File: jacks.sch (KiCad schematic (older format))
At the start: 73 parts, among them J1 PJ301CM, J10 PJ301BM, J11 PJ301BM, J12 PJ301BM, J13 PJ301BM, J14 PJ301BM, J15 PJ301BM, J16 PJ301BM, J17 PJ301BM, J18 PJ301BM, J19 PJ301BM, J2 PJ301CM, J20 PJ301BM, J21 PJ301BM, J22 PJ301BM, J23 PJ301BM, J24 PJ301BM, J25 PJ301BM, J26 PJ301BM, J3 PJ301BM, J4 PJ301BM, J5 PJ301BM, J6 PJ301BM, J7 PJ301BM, J8 PJ301BM, J9 PJ301BM, Q1 MMBT3904, Q2 MMBT3904, Q3 MMBT3904, Q4 MMBT3904, U1 VO0600T, U2 74LV1T34, U6 MCP6004

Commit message: updated footprints
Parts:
- J1, J2: footprint w_connector:PJ301CM_OFFSET -> w_connector:PJ366ST_Compact
- J10, J11, J12, J13, J14, J15, J16, J17, J18, J19, J20, J21, J22, J23, J24, J25, J26, J3, J4, J5, J6, J7, J8, J9: footprint w_connector:PJ301BM -> w_connector:PJ301M-12_Compact
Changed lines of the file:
@@
 F 0 "J3" H 900 1600 50  0000 C CNN
 F 1 "PJ301BM" H 900 2000 50  0000 C CNN
-F 2 "w_connector:PJ301BM" H 1250 1900 50  0001 C CNN
+F 2 "w_connector:PJ301M-12_Compact" H 1250 1900 50  0001 C CNN
 F 3 "http://www.qingpu-electronics.com/en/products/wqp-pj3010bm-34.html" H 1250 1900 50  0001 C CNN
 F 4 "Wenzhou QingPu Electronics" H 900 1700 50  0001 C CNN "MFN"
@@
 F 0 "J4" H 900 3200 50  0000 C CNN
 F 1 "PJ301BM" H 900 3600 50  0000 C CNN
-F 2 "w_connector:PJ301BM" H 1250 3500 50  0001 C CNN
+F 2 "w_connector:PJ301M-12_Compact" H 1250 3500 50  0001 C CNN
 F 3 "http://www.qingpu-electronics.com/en/products/wqp-pj3010bm-34.html" H 1250 3500 50  0001 C CNN
 F 4 "Wenzhou QingPu Electronics" H 900 3300 50  0001 C CNN "MFN"
@@
 F 0 "J5" H 4700 1300 50  0000 C CNN
 F 1 "PJ301BM" H 4700 1700 50  0000 C CNN
-F 2 "w_connector:PJ301BM" H 5050 1600 50  0001 C CNN
+F 2 "w_connector:PJ301M-12_Compact" H 5050 1600 50  0001 C CNN
 F 3 "http://www.qingpu-electronics.com/en/products/wqp-pj3010bm-34.html" H 5050 1600 50  0001 C CNN
 F 4 "Wenzhou QingPu Electronics" H 4700 1400 50  0001 C CNN "MFN"
@@
 F 0 "J6" H 4700 3000 50  0000 C CNN
 F 1 "PJ301BM" H 4700 3400 50  0000 C CNN
-F 2 "w_connector:PJ301BM" H 5050 3300 50  0001 C CNN
+F 2 "w_connector:PJ301M-12_Compact" H 5050 3300 50  0001 C CNN
 F 3 "http://www.qingpu-electronics.com/en/products/wqp-pj3010bm-34.html" H 5050 3300 50  0001 C CNN
 F 4 "Wenzhou QingPu Electronics" H 4700 3100 50  0001 C CNN "MFN"
@@
 F 0 "J12" H 8800 700 50  0000 C CNN
 F 1 "PJ301BM" H 8800 1100 50  0000 C CNN
-F 2 "w_connector:PJ301BM" H 9150 1000 50  0001 C CNN
+F 2 "w_connector:PJ301M-12_Compact" H 9150 1000 50  0001 C CNN
 F 3 "http://www.qingpu-electronics.com/en/products/wqp-pj3010bm-34.html" H 9150 1000 50  0001 C CNN
 F 4 "Wenzhou QingPu Electronics" H 8800 800 50  0001 C CNN "MFN"
@@
 F 0 "J14" H 8800 1400 50  0000 C CNN
 F 1 "PJ301BM" H 8800 1800 50  0000 C CNN
-F 2 "w_connector:PJ301BM" H 9150 1700 50  0001 C CNN
+F 2 "w_connector:PJ301M-12_Compact" H 9150 1700 50  0001 C CNN
 F 3 "http://www.qingpu-electronics.com/en/products/wqp-pj3010bm-34.html" H 9150 1700 50  0001 C CNN
 F 4 "Wenzhou QingPu Electronics" H 8800 1500 50  0001 C CNN "MFN"
@@
 F 0 "J16" H 8800 2100 50  0000 C CNN
 F 1 "PJ301BM" H 8800 2500 50  0000 C CNN
-F 2 "w_connector:PJ301BM" H 9150 2400 50  0001 C CNN
+F 2 "w_connector:PJ301M-12_Compact" H 9150 2400 50  0001 C CNN
 F 3 "http://www.qingpu-electronics.com/en/products/wqp-pj3010bm-34.html" H 9150 2400 50  0001 C CNN
 F 4 "Wenzhou QingPu Electronics" H 8800 2200 50  0001 C CNN "MFN"
@@
 F 0 "J18" H 8800 2800 50  0000 C CNN
 F 1 "PJ301BM" H 8800 3200 50  0000 C CNN
-F 2 "w_connector:PJ301BM" H 9150 3100 50  0001 C CNN
+F 2 "w_connector:PJ301M-12_Compact" H 9150 3100 50  0001 C CNN
 F 3 "http://www.qingpu-electronics.com/en/products/wqp-pj3010bm-34.html" H 9150 3100 50  0001 C CNN
 F 4 "Wenzhou QingPu Electronics" H 8800 2900 50  0001 C CNN "MFN"
@@
 F 0 "J20" H 8800 3500 50  0000 C CNN
 F 1 "PJ301BM" H 8800 3900 50  0000 C CNN
-F 2 "w_connector:PJ301BM" H 9150 3800 50  0001 C CNN
+F 2 "w_connector:PJ301M-12_Compact" H 9150 3800 50  0001 C CNN
 F 3 "http://www.qingpu-electronics.com/en/products/wqp-pj3010bm-34.html" H 9150 3800 50  0001 C CNN
 F 4 "Wenzhou QingPu Electronics" H 8800 3600 50  0001 C CNN "MFN"
@@
 F 0 "J22" H 8800 4200 50  0000 C CNN
 F 1 "PJ301BM" H 8800 4600 50  0000 C CNN
-F 2 "w_connector:PJ301BM" H 9150 4500 50  0001 C CNN
+F 2 "w_connector:PJ301M-12_Compact" H 9150 4500 50  0001 C CNN
 F 3 "http://www.qingpu-electronics.com/en/products/wqp-pj3010bm-34.html" H 9150 4500 50  0001 C CNN
 F 4 "Wenzhou QingPu Electronics" H 8800 4300 50  0001 C CNN "MFN"
@@
 F 0 "J24" H 8800 4900 50  0000 C CNN
 F 1 "PJ301BM" H 8800 5300 50  0000 C CNN
-F 2 "w_connector:PJ301BM" H 9150 5200 50  0001 C CNN
+F 2 "w_connector:PJ301M-12_Compact" H 9150 5200 50  0001 C CNN
 F 3 "http://www.qingpu-electronics.com/en/products/wqp-pj3010bm-34.html" H 9150 5200 50  0001 C CNN
 F 4 "Wenzhou QingPu Electronics" H 8800 5000 50  0001 C CNN "MFN"
@@
 F 0 "J26" H 8800 5600 50  0000 C CNN
 F 1 "PJ301BM" H 8800 6000 50  0000 C CNN
-F 2 "w_connector:PJ301BM" H 9150 5900 50  0001 C CNN
+F 2 "w_connector:PJ301M-12_Compact" H 9150 5900 50  0001 C CNN
 F 3 "http://www.qingpu-electronics.com/en/products/wqp-pj3010bm-34.html" H 9150 5900 50  0001 C CNN
 F 4 "Wenzhou QingPu Electronics" H 8800 5700 50  0001 C CNN "MFN"
@@
 F 0 "J11" H 10400 700 50  0000 C CNN
 F 1 "PJ301BM" H 10400 1100 50  0000 C CNN
-F 2 "w_connector:PJ301BM" H 10750 1000 50  0001 C CNN
+F 2 "w_connector:PJ301M-12_Compact" H 10750 1000 50  0001 C CNN
 F 3 "http://www.qingpu-electronics.com/en/products/wqp-pj3010bm-34.html" H 10750 1000 50  0001 C CNN
 F 4 "Wenzhou QingPu Electronics" H 10400 800 50  0001 C CNN "MFN"
@@
 F 0 "J13" H 10400 1400 50  0000 C CNN
 F 1 "PJ301BM" H 10400 1800 50  0000 C CNN
-F 2 "w_connector:PJ301BM" H 10750 1700 50  0001 C CNN
+F 2 "w_connector:PJ301M-12_Compact" H 10750 1700 50  0001 C CNN
 F 3 "http://www.qingpu-electronics.com/en/products/wqp-pj3010bm-34.html" H 10750 1700 50  0001 C CNN
 F 4 "Wenzhou QingPu Electronics" H 10400 1500 50  0001 C CNN "MFN"
@@
 F 0 "J15" H 10400 2100 50  0000 C CNN
 F 1 "PJ301BM" H 10400 2500 50  0000 C CNN
-F 2 "w_connector:PJ301BM" H 10750 2400 50  0001 C CNN
+F 2 "w_connector:PJ301M-12_Compact" H 10750 2400 50  0001 C CNN
 F 3 "http://www.qingpu-electronics.com/en/products/wqp-pj3010bm-34.html" H 10750 2400 50  0001 C CNN
 F 4 "Wenzhou QingPu Electronics" H 10400 2200 50  0001 C CNN "MFN"
@@
 F 0 "J17" H 10400 2800 50  0000 C CNN
 F 1 "PJ301BM" H 10400 3200 50  0000 C CNN
-F 2 "w_connector:PJ301BM" H 10750 3100 50  0001 C CNN
+F 2 "w_connector:PJ301M-12_Compact" H 10750 3100 50  0001 C CNN
 F 3 "http://www.qingpu-electronics.com/en/products/wqp-pj3010bm-34.html" H 10750 3100 50  0001 C CNN
 F 4 "Wenzhou QingPu Electronics" H 10400 2900 50  0001 C CNN "MFN"
@@
 F 0 "J19" H 10400 3500 50  0000 C CNN
 F 1 "PJ301BM" H 10400 3900 50  0000 C CNN
-F 2 "w_connector:PJ301BM" H 10750 3800 50  0001 C CNN
+F 2 "w_connector:PJ301M-12_Compact" H 10750 3800 50  0001 C CNN
 F 3 "http://www.qingpu-electronics.com/en/products/wqp-pj3010bm-34.html" H 10750 3800 50  0001 C CNN
 F 4 "Wenzhou QingPu Electronics" H 10400 3600 50  0001 C CNN "MFN"
@@
 F 0 "J21" H 10400 4200 50  0000 C CNN
 F 1 "PJ301BM" H 10400 4600 50  0000 C CNN
-F 2 "w_connector:PJ301BM" H 10750 4500 50  0001 C CNN
+F 2 "w_connector:PJ301M-12_Compact" H 10750 4500 50  0001 C CNN
 F 3 "http://www.qingpu-electronics.com/en/products/wqp-pj3010bm-34.html" H 10750 4500 50  0001 C CNN
 F 4 "Wenzhou QingPu Electronics" H 10400 4300 50  0001 C CNN "MFN"
@@
 F 0 "J23" H 10400 4900 50  0000 C CNN
 F 1 "PJ301BM" H 10400 5300 50  0000 C CNN
-F 2 "w_connector:PJ301BM" H 10750 5200 50  0001 C CNN
+F 2 "w_connector:PJ301M-12_Compact" H 10750 5200 50  0001 C CNN
 F 3 "http://www.qingpu-electronics.com/en/products/wqp-pj3010bm-34.html" H 10750 5200 50  0001 C CNN
 F 4 "Wenzhou QingPu Electronics" H 10400 5000 50  0001 C CNN "MFN"
@@
 F 0 "J25" H 10400 5600 50  0000 C CNN
 F 1 "PJ301BM" H 10400 6000 50  0000 C CNN
-F 2 "w_connector:PJ301BM" H 10750 5900 50  0001 C CNN
+F 2 "w_connector:PJ301M-12_Compact" H 10750 5900 50  0001 C CNN
 F 3 "http://www.qingpu-electronics.com/en/products/wqp-pj3010bm-34.html" H 10750 5900 50  0001 C CNN
 F 4 "Wenzhou QingPu Electronics" H 10400 5700 50  0001 C CNN "MFN"
@@
 F 0 "J7" H 900 5000 50  0000 C CNN
 F 1 "PJ301BM" H 900 5400 50  0000 C CNN
-F 2 "w_connector:PJ301BM" H 1250 5300 50  0001 C CNN
+F 2 "w_connector:PJ301M-12_Compact" H 1250 5300 50  0001 C CNN
 F 3 "http://www.qingpu-electronics.com/en/products/wqp-pj3010bm-34.html" H 1250 5300 50  0001 C CNN
 F 4 "Wenzhou QingPu Electronics" H 900 5100 50  0001 C CNN "MFN"
@@
 F 0 "J8" H 900 6500 50  0000 C CNN
 F 1 "PJ301BM" H 900 6900 50  0000 C CNN
-F 2 "w_connector:PJ301BM" H 1250 6800 50  0001 C CNN
+F 2 "w_connector:PJ301M-12_Compact" H 1250 6800 50  0001 C CNN
 F 3 "http://www.qingpu-electronics.com/en/products/wqp-pj3010bm-34.html" H 1250 6800 50  0001 C CNN
 F 4 "Wenzhou QingPu Electronics" H 900 6600 50  0001 C CNN "MFN"
@@
 F 0 "J9" H 3300 5000 50  0000 C CNN
 F 1 "PJ301BM" H 3300 5400 50  0000 C CNN
-F 2 "w_connector:PJ301BM" H 3650 5300 50  0001 C CNN
+F 2 "w_connector:PJ301M-12_Compact" H 3650 5300 50  0001 C CNN
 F 3 "http://www.qingpu-electronics.com/en/products/wqp-pj3010bm-34.html" H 3650 5300 50  0001 C CNN
 F 4 "Wenzhou QingPu Electronics" H 3300 5100 50  0001 C CNN "MFN"
@@
 F 0 "J10" H 3300 6500 50  0000 C CNN
 F 1 "PJ301BM" H 3300 6900 50  0000 C CNN
-F 2 "w_connector:PJ301BM" H 3650 6800 50  0001 C CNN
+F 2 "w_connector:PJ301M-12_Compact" H 3650 6800 50  0001 C CNN
 F 3 "http://www.qingpu-electronics.com/en/products/wqp-pj3010bm-34.html" H 3650 6800 50  0001 C CNN
 F 4 "Wenzhou QingPu Electronics" H 3300 6600 50  0001 C CNN "MFN"
@@
 F 0 "J1" H 5800 1300 50  0000 C CNN
 F 1 "PJ301CM" H 5800 1700 50  0000 C CNN
-F 2 "w_connector:PJ301CM_OFFSET" H 6150 1600 50  0001 C CNN
+F 2 "w_connector:PJ366ST_Compact" H 6150 1600 50  0001 C CNN
 F 3 "http://www.qingpu-electronics.com/en/products/WQP-PJ301CM-40.html" H 6150 1600 50  0001 C CNN
 F 4 "Wenzhou QingPu Electronics" H 5800 1400 50  0001 C CNN "MFN"
@@
 F 0 "J2" H 7600 3100 50  0000 C CNN
 F 1 "PJ301CM" H 7600 3500 50  0000 C CNN
-F 2 "w_connector:PJ301CM_OFFSET" H 7950 3400 50  0001 C CNN
+F 2 "w_connector:PJ366ST_Compact" H 7950 3400 50  0001 C CNN
 F 3 "http://www.qingpu-electronics.com/en/products/WQP-PJ301CM-40.html" H 7950 3400 50  0001 C CNN
 F 4 "Wenzhou QingPu Electronics" H 7600 3200 50  0001 C CNN "MFN"

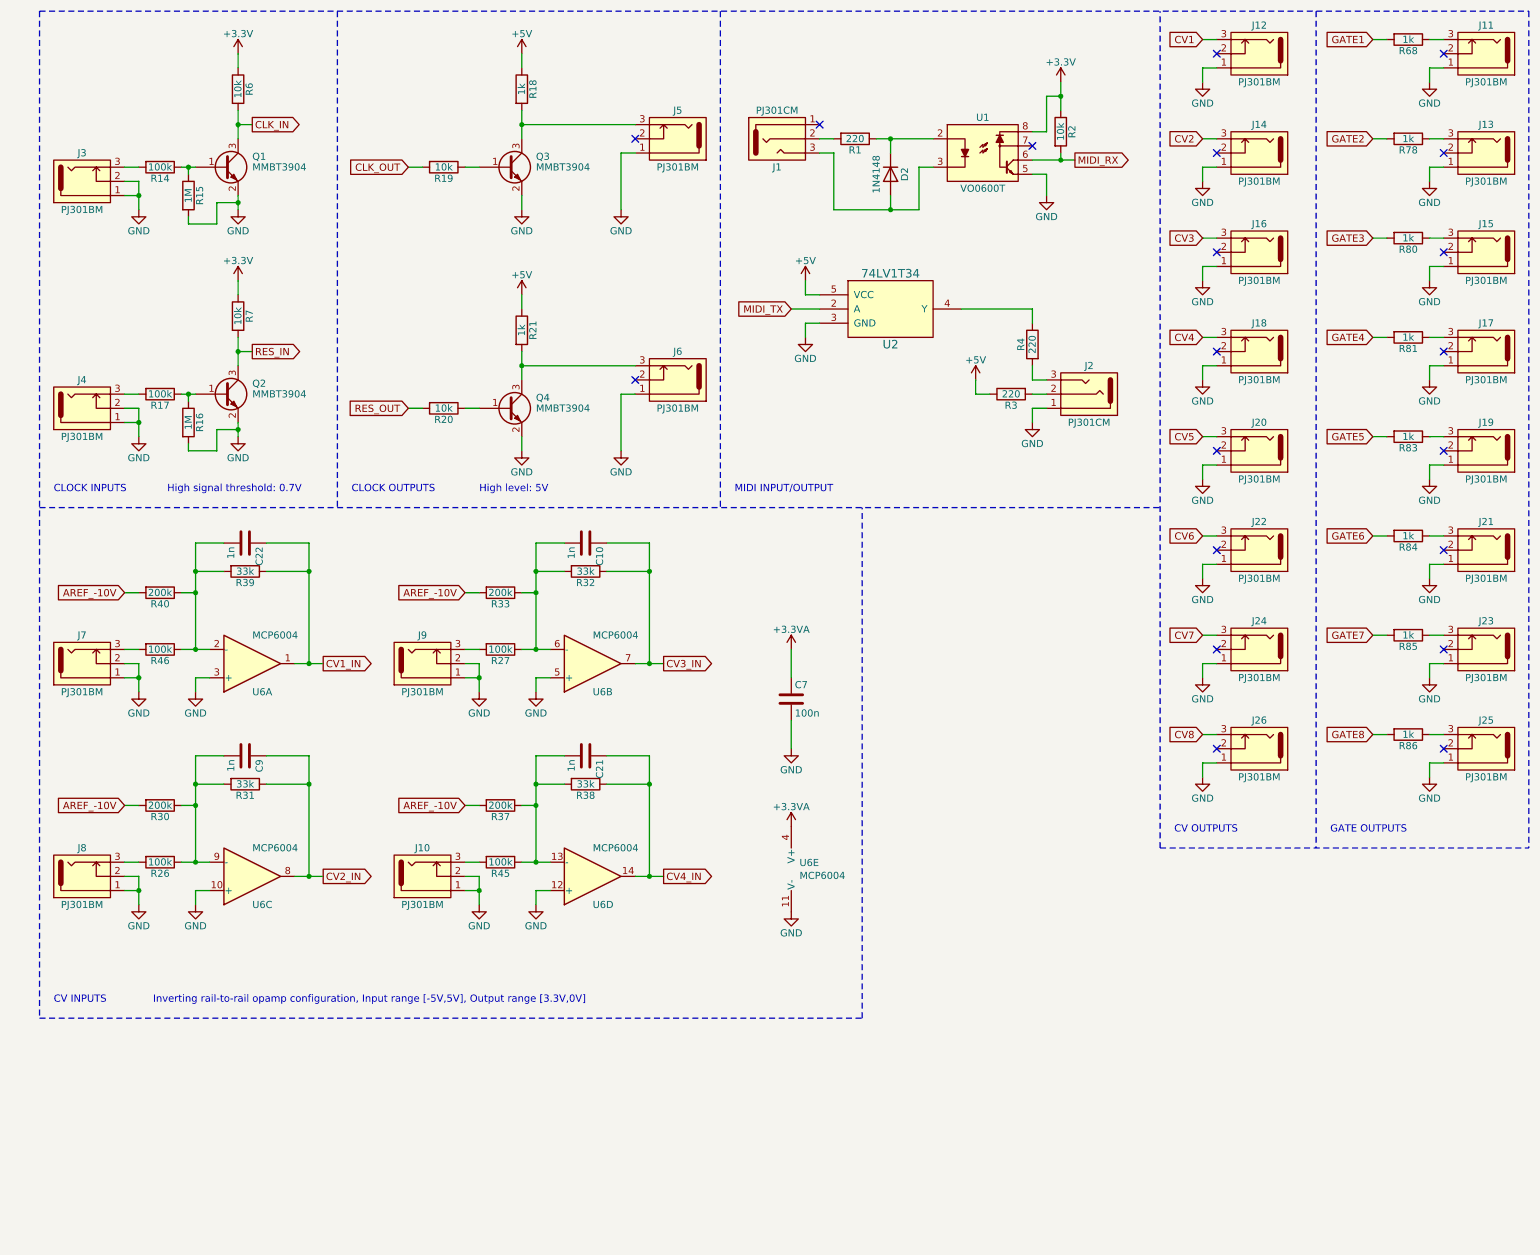
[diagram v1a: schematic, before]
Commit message: updated component values and revision
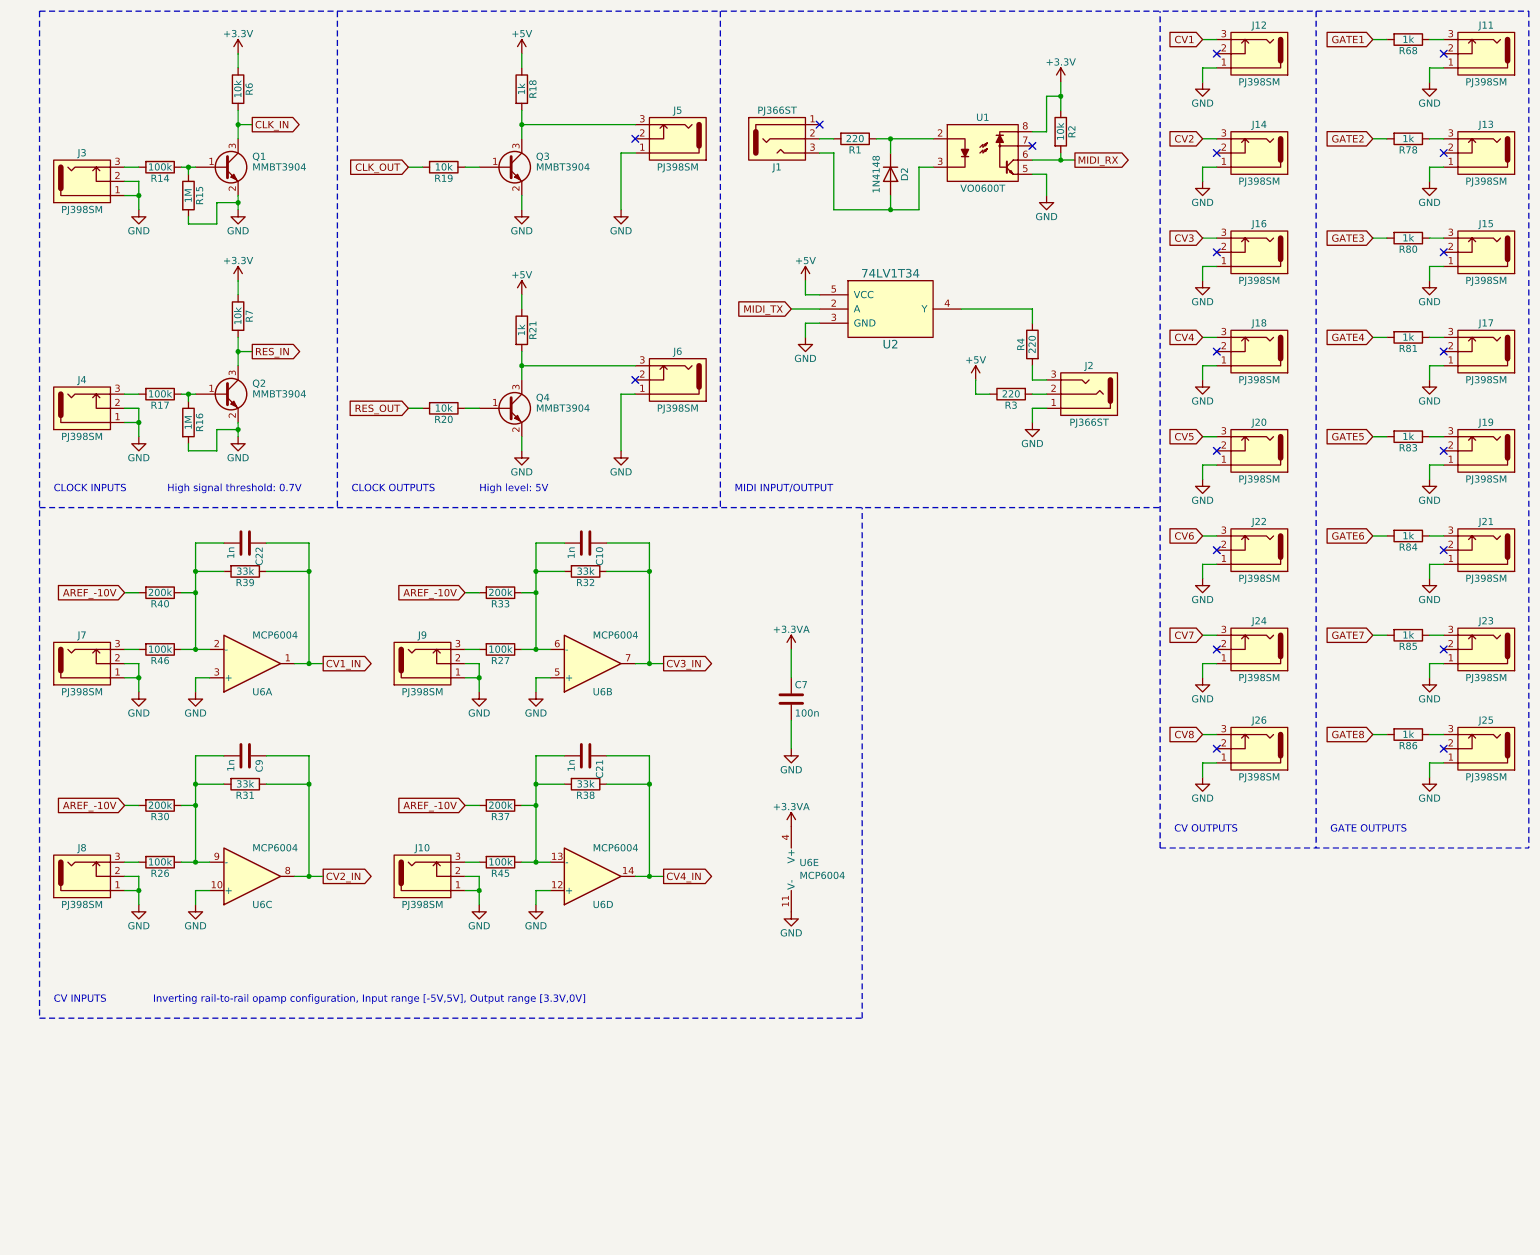
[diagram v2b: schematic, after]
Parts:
- J1, J2: value PJ301CM -> PJ366ST; MFP WQP-PJ301CM -> WQP-PJ366ST
- J10, J11, J12, J13, J14, J15, J16, J17, J18, J19, J20, J21, J22, J23, J24, J25, J26, J3, J4, J5, J6, J7, J8, J9: value PJ301BM -> PJ398SM; MFP WQP-PJ301BM -> WQP-PJ398SM
- U6: MFN (none) -> Microchip; MFP (none) -> MCP6004-I/SL; Package (none) -> SOIC-14

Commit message: add voltage supervisor, add leds to jacks, update footprints
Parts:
- added D42, D43, D44, D45, D46, D47, D48, D49, D50, D51, D52, D53, D54, D55, D56, D57, D58, D59, D60, D61, D62, D63, D64, D65, D66, D67: LED, w_capacitor:C_1206, symbol Device:LED
- added R100, R101, R102, R103, R104, R105, R106, R107, R108, R109, R110, R111, R112, R87, R88, R89, R90, R91, R92, R93, R94, R95, R96, R97, R98, R99: 1k, w_resistor:R_0603, symbol Device:R
- J10, J11, J12, J13, J14, J15, J16, J17, J18, J19, J20, J21, J22, J23, J24, J25, J26, J3, J4, J5, J6, J7, J8, J9: footprint w_connector:PJ301M-12_Compact -> w_connector:jack_thonk
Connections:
- net labels added: +12V
- wire segments 235 -> 250
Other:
- moved on the sheet: C7, U6E

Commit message: small changes
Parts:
- added C51, C52, C53, C54: ESD, w_capacitor:C_0603, symbol Device:C
- added D68, D69: 1N4148WS, Diode_SMD:D_SOD-123, symbol Diode:1N4148WS
- added J27: Conn_01x03_Female, Connector_PinHeader_2.54mm:PinHeader_1x03_P2.54mm_Vertical, symbol Connector:Conn_01x03_Female
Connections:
- net labels added: LED_VDD
- wire segments 250 -> 273
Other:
- moved on the sheet: D2, J1, J10, J2, J7, J8, J9, R1, R2, R26, R3, R4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
